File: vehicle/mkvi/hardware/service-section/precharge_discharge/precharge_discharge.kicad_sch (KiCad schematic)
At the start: 13 parts, among them J1 MicroFit_VT_5x1, J2 Automotive_M.2_Edge_Connector, K1 G2RG-2A-X_DC12, K2 3350-4275-126, Q1 SSM3K333R

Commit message: Begin layout add footprints
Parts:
- K1: footprint OEM:G2RG-2A-X -> OEM:G2RG-X
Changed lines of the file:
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@@
     (property "Reference" "K1" (id 0) (at 71.12 43.18 0))
     (property "Value" "G2RG-2A-X_DC12" (id 1) (at 71.12 45.72 0))
-    (property "Footprint" "OEM:G2RG-2A-X" (id 2) (at 71.12 57.15 0)
+    (property "Footprint" "OEM:G2RG-X" (id 2) (at 71.12 57.15 0)
       (effects (font (size 1.27 1.27)) hide)
     )
@@
       (reference "#PWR?") (unit 1) (value "GND") (footprint "")
     )
-    (path "/1d3603a0-934c-404e-9b38-4b65044f588c/607af4f2-91e7-418d-a7ac-4d54e191778d"
-      (reference "C1") (unit 1) (value "10nF") (footprint "")
-    )
-    (path "/aae00dc5-0627-4ce2-bb50-5359aef1b906/607af4f2-91e7-418d-a7ac-4d54e191778d"
-      (reference "C2") (unit 1) (value "10nF") (footprint "")
-    )
-    (path "/f42ceb10-3a39-4caa-a323-2ed850359949/607af4f2-91e7-418d-a7ac-4d54e191778d"
-      (reference "C3") (unit 1) (value "10nF") (footprint "")
+    (path "/1d3603a0-934c-404e-9b38-4b65044f588c/6dc3a5a5-6ba7-45ee-890e-2b247ac5cbfa"
+      (reference "C1") (unit 1) (value "C_10nF") (footprint "footprints:C_1206_OEM")
+    )
+    (path "/aae00dc5-0627-4ce2-bb50-5359aef1b906/6dc3a5a5-6ba7-45ee-890e-2b247ac5cbfa"
+      (reference "C2") (unit 1) (value "C_10nF") (footprint "footprints:C_1206_OEM")
+    )
+    (path "/f42ceb10-3a39-4caa-a323-2ed850359949/6dc3a5a5-6ba7-45ee-890e-2b247ac5cbfa"
+      (reference "C3") (unit 1) (value "C_10nF") (footprint "footprints:C_1206_OEM")
     )
     (path "/13199f4f-49d4-4127-8a75-8da39b0b7cb9"
@@
     )
     (path "/06e0ac0e-a0c5-4a6c-9061-994da59b167d"
-      (reference "K1") (unit 1) (value "G2RG-2A-X_DC12") (footprint "OEM:G2RG-2A-X")
+      (reference "K1") (unit 1) (value "G2RG-2A-X_DC12") (footprint "OEM:G2RG-X")
     )
     (path "/1c839dd3-e0c7-4808-b8be-0e8fc2ef2cdb"
@@
     )
     (path "/1d3603a0-934c-404e-9b38-4b65044f588c/ca7852e4-64fa-4c30-bad9-fbe9a1ffbb05"
-      (reference "TH1") (unit 1) (value "Thermistor") (footprint "")
+      (reference "TH1") (unit 1) (value "Thermistor") (footprint "footprints:Thermistor")
     )
     (path "/aae00dc5-0627-4ce2-bb50-5359aef1b906/ca7852e4-64fa-4c30-bad9-fbe9a1ffbb05"
-      (reference "TH2") (unit 1) (value "Thermistor") (footprint "")
+      (reference "TH2") (unit 1) (value "Thermistor") (footprint "footprints:Thermistor")
     )
     (path "/f42ceb10-3a39-4caa-a323-2ed850359949/ca7852e4-64fa-4c30-bad9-fbe9a1ffbb05"
-      (reference "TH3") (unit 1) (value "Thermistor") (footprint "")
+      (reference "TH3") (unit 1) (value "Thermistor") (footprint "footprints:Thermistor")
     )
     (path "/1d3603a0-934c-404e-9b38-4b65044f588c/1d731957-08e8-4a84-bf4b-f84aa0692269"

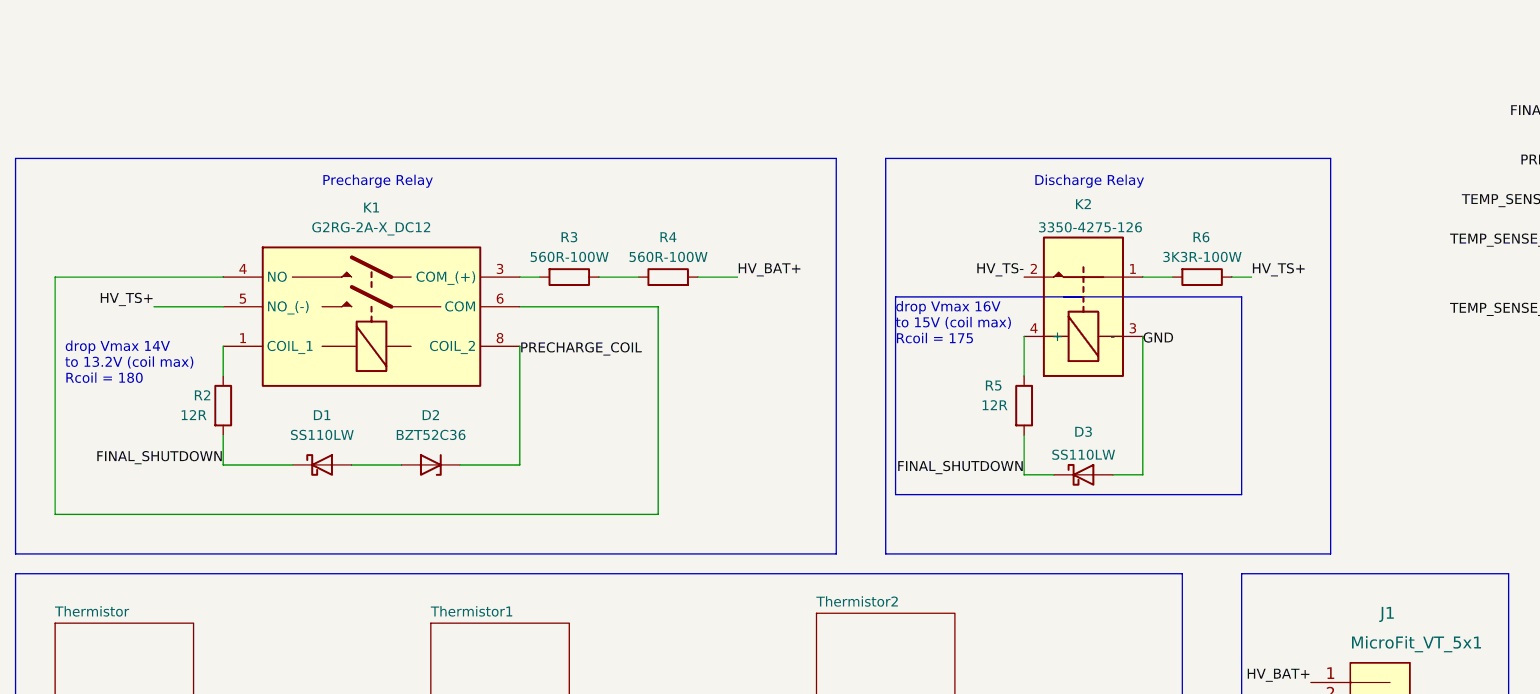
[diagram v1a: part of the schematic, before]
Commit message: Rev.3 Precharge_Discharge Schematic
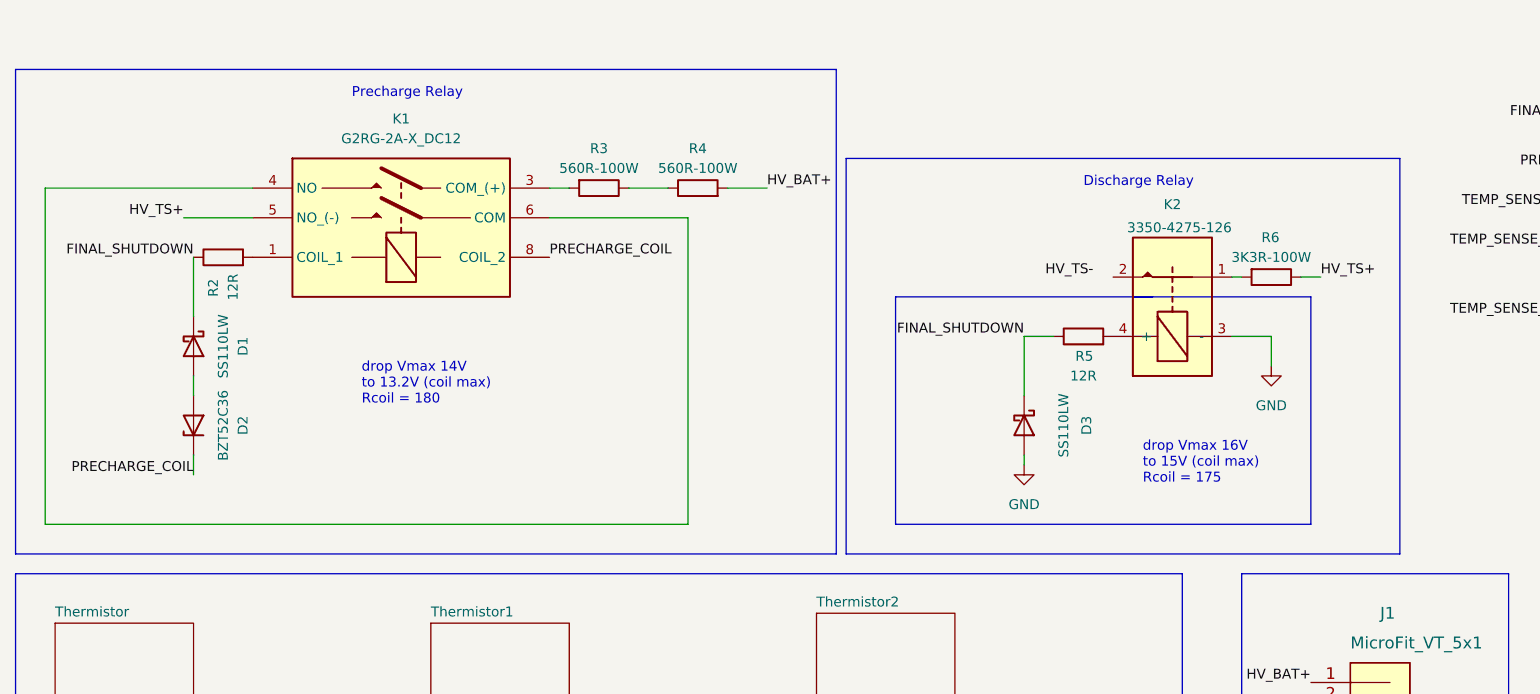
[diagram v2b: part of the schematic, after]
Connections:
- net FINAL_SHUTDOWN: now also R2.1, R5.1; no longer R2.2, R5.2
- net HV_TS-: no longer K2.2
- net at K1.1 (COIL_1): now also R2.2; no longer R2.1
- net at K2.4 (+): now also R5.2; no longer R5.1
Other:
- moved on the sheet: D1, D2, D3, K1, K2, R2, R3, R4, R5, R6

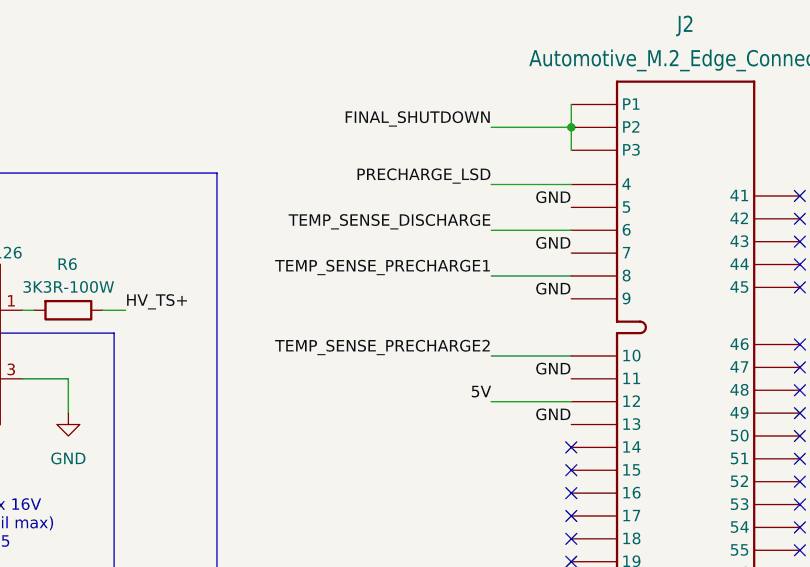
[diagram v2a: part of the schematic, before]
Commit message: V1. Precharge_Discharge PCB Layout
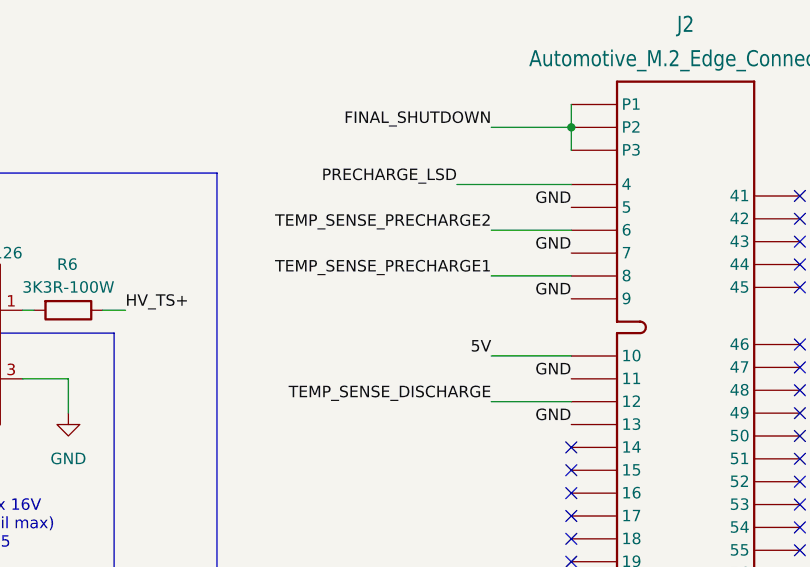
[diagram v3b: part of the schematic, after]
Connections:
- net +5V: now also J2.10; no longer J2.12
- net TEMP_SENSE_DISCHARGE: now also J2.12; no longer J2.6
- net TEMP_SENSE_PRECHARGE2: now also J2.6; no longer J2.10
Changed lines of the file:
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@@
     (stroke (width 0) (type default) (color 0 0 0 0))
   )
-  (wire (pts (xy 233.68 38.1) (xy 242.57 38.1))
+  (wire (pts (xy 229.87 38.1) (xy 242.57 38.1))
     (stroke (width 0) (type default) (color 0 0 0 0))
   )
@@
     (effects (font (size 1.27 1.27)) (justify left bottom))
   )
-  (label "5V" (at 233.68 62.23 180)
+  (label "TEMP_SENSE_DISCHARGE" (at 233.68 62.23 180)
     (effects (font (size 1.27 1.27)) (justify right bottom))
   )
@@
     (effects (font (size 1.27 1.27)) (justify right bottom))
   )
-  (label "TEMP_SENSE_DISCHARGE" (at 233.68 43.18 180)
+  (label "TEMP_SENSE_PRECHARGE2" (at 233.68 43.18 180)
     (effects (font (size 1.27 1.27)) (justify right bottom))
   )
@@
     (effects (font (size 1.27 1.27)) (justify left bottom))
   )
-  (label "TEMP_SENSE_PRECHARGE2" (at 233.68 57.15 180)
+  (label "5V" (at 233.68 57.15 180)
     (effects (font (size 1.27 1.27)) (justify right bottom))
   )
@@
     (effects (font (size 1.27 1.27)) (justify right bottom))
   )
-  (label "PRECHARGE_LSD" (at 233.68 38.1 180)
-    (effects (font (size 1.27 1.27)) (justify right bottom))
-  )
+  (label "PRECHARGE_LSD" (at 229.87 38.1 180)
+    (effects (font (size 1.27 1.27)) (justify right bottom))
+  )

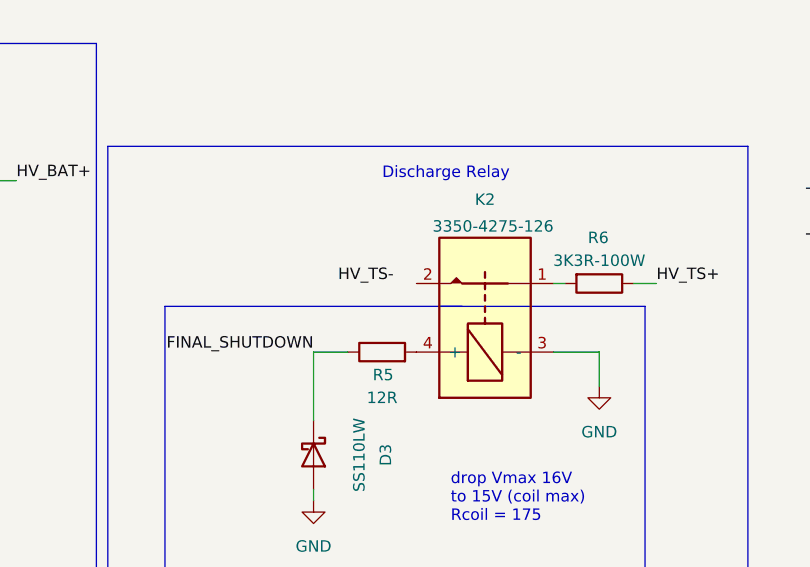
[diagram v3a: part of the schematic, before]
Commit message: feat: updates from layout checklist
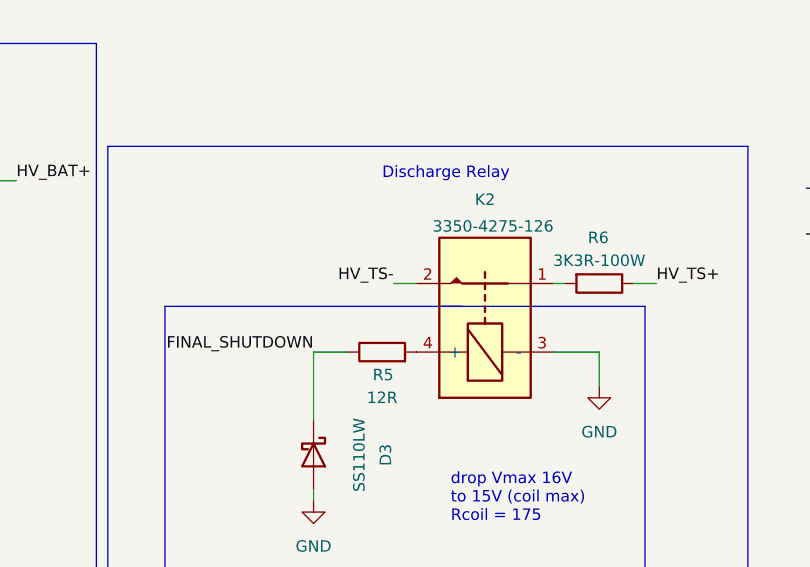
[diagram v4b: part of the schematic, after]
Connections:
- net HV_TS-: now also K2.2
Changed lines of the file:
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@@
+    (stroke (width 0) (type default) (color 0 0 0 0))
+  )
+  (wire (pts (xy 163.83 52.07) (xy 166.37 52.07))
     (stroke (width 0) (type default) (color 0 0 0 0))
   )
@@
   )
   (symbol_instances
+    (path "/61fcfc8d-80a4-4ffc-b730-9f17fc90d2e2"
+      (reference "#PWR?") (unit 1) (value "GND") (footprint "")
+    )
+    (path "/4e074b05-b4d4-46e8-b6a4-6079f1f04f3c"
+      (reference "#PWR?") (unit 1) (value "GND") (footprint "")
+    )
+    (path "/39fb457f-45e0-4faa-b286-55e2425f34ba"
+      (reference "#PWR?") (unit 1) (value "GND") (footprint "")
+    )
     (path "/18930298-950b-43f3-992d-121e7a00145a"
       (reference "#PWR?") (unit 1) (value "GND") (footprint "")
@@
       (reference "#PWR?") (unit 1) (value "+5V") (footprint "")
     )
-    (path "/39fb457f-45e0-4faa-b286-55e2425f34ba"
-      (reference "#PWR?") (unit 1) (value "GND") (footprint "")
+    (path "/1d3603a0-934c-404e-9b38-4b65044f588c/a178f5c8-b4bb-4143-aeb6-2cae7a246fa0"
+      (reference "#PWR?") (unit 1) (value "+5V") (footprint "")
     )
     (path "/1d3603a0-934c-404e-9b38-4b65044f588c/80d772a7-c654-45d6-8d16-7b789d3c1039"
       (reference "#PWR?") (unit 1) (value "+5V") (footprint "")
     )
-    (path "/1d3603a0-934c-404e-9b38-4b65044f588c/a178f5c8-b4bb-4143-aeb6-2cae7a246fa0"
+    (path "/1d3603a0-934c-404e-9b38-4b65044f588c/a2a80cf1-64e7-4004-9710-deb7f131cb2a"
+      (reference "#PWR?") (unit 1) (value "GND") (footprint "")
+    )
+    (path "/1d3603a0-934c-404e-9b38-4b65044f588c/ab021d4c-2de5-4da2-b018-19ab9a4b838b"
+      (reference "#PWR?") (unit 1) (value "GND") (footprint "")
+    )
+    (path "/1d3603a0-934c-404e-9b38-4b65044f588c/3b9fedc3-8004-49ad-a3fe-28afa1ea394b"
+      (reference "#PWR?") (unit 1) (value "GND") (footprint "")
+    )
+    (path "/aae00dc5-0627-4ce2-bb50-5359aef1b906/a178f5c8-b4bb-4143-aeb6-2cae7a246fa0"
       (reference "#PWR?") (unit 1) (value "+5V") (footprint "")
-    )
-    (path "/1d3603a0-934c-404e-9b38-4b65044f588c/a2a80cf1-64e7-4004-9710-deb7f131cb2a"
-      (reference "#PWR?") (unit 1) (value "GND") (footprint "")
-    )
-    (path "/1d3603a0-934c-404e-9b38-4b65044f588c/ab021d4c-2de5-4da2-b018-19ab9a4b838b"
-      (reference "#PWR?") (unit 1) (value "GND") (footprint "")
-    )
-    (path "/1d3603a0-934c-404e-9b38-4b65044f588c/3b9fedc3-8004-49ad-a3fe-28afa1ea394b"
-      (reference "#PWR?") (unit 1) (value "GND") (footprint "")
     )
     (path "/aae00dc5-0627-4ce2-bb50-5359aef1b906/80d772a7-c654-45d6-8d16-7b789d3c1039"
       (reference "#PWR?") (unit 1) (value "+5V") (footprint "")
     )
-    (path "/aae00dc5-0627-4ce2-bb50-5359aef1b906/a178f5c8-b4bb-4143-aeb6-2cae7a246fa0"
+    (path "/aae00dc5-0627-4ce2-bb50-5359aef1b906/a2a80cf1-64e7-4004-9710-deb7f131cb2a"
+      (reference "#PWR?") (unit 1) (value "GND") (footprint "")
+    )
+    (path "/aae00dc5-0627-4ce2-bb50-5359aef1b906/ab021d4c-2de5-4da2-b018-19ab9a4b838b"
+      (reference "#PWR?") (unit 1) (value "GND") (footprint "")
+    )
+    (path "/aae00dc5-0627-4ce2-bb50-5359aef1b906/3b9fedc3-8004-49ad-a3fe-28afa1ea394b"
+      (reference "#PWR?") (unit 1) (value "GND") (footprint "")
+    )
+    (path "/f42ceb10-3a39-4caa-a323-2ed850359949/a178f5c8-b4bb-4143-aeb6-2cae7a246fa0"
       (reference "#PWR?") (unit 1) (value "+5V") (footprint "")
-    )
-    (path "/aae00dc5-0627-4ce2-bb50-5359aef1b906/a2a80cf1-64e7-4004-9710-deb7f131cb2a"
-      (reference "#PWR?") (unit 1) (value "GND") (footprint "")
-    )
-    (path "/aae00dc5-0627-4ce2-bb50-5359aef1b906/ab021d4c-2de5-4da2-b018-19ab9a4b838b"
-      (reference "#PWR?") (unit 1) (value "GND") (footprint "")
-    )
-    (path "/aae00dc5-0627-4ce2-bb50-5359aef1b906/3b9fedc3-8004-49ad-a3fe-28afa1ea394b"
-      (reference "#PWR?") (unit 1) (value "GND") (footprint "")
     )
     (path "/f42ceb10-3a39-4caa-a323-2ed850359949/80d772a7-c654-45d6-8d16-7b789d3c1039"
       (reference "#PWR?") (unit 1) (value "+5V") (footprint "")
     )
-    (path "/f42ceb10-3a39-4caa-a323-2ed850359949/a178f5c8-b4bb-4143-aeb6-2cae7a246fa0"
-      (reference "#PWR?") (unit 1) (value "+5V") (footprint "")
-    )
     (path "/f42ceb10-3a39-4caa-a323-2ed850359949/a2a80cf1-64e7-4004-9710-deb7f131cb2a"
       (reference "#PWR?") (unit 1) (value "GND") (footprint "")
@@
       (reference "#PWR?") (unit 1) (value "GND") (footprint "")
     )
-    (path "/4e074b05-b4d4-46e8-b6a4-6079f1f04f3c"
-      (reference "#PWR?") (unit 1) (value "GND") (footprint "")
-    )
-    (path "/61fcfc8d-80a4-4ffc-b730-9f17fc90d2e2"
+    (path "/1d3603a0-934c-404e-9b38-4b65044f588c/90dd3af5-4ce0-4209-b124-e700e1d8b918"
+      (reference "#PWR?") (unit 1) (value "GND") (footprint "")
+    )
+    (path "/aae00dc5-0627-4ce2-bb50-5359aef1b906/90dd3af5-4ce0-4209-b124-e700e1d8b918"
+      (reference "#PWR?") (unit 1) (value "GND") (footprint "")
+    )
+    (path "/f42ceb10-3a39-4caa-a323-2ed850359949/90dd3af5-4ce0-4209-b124-e700e1d8b918"
       (reference "#PWR?") (unit 1) (value "GND") (footprint "")
     )
@@
       (reference "C3") (unit 1) (value "C_10nF") (footprint "footprints:C_1206_OEM")
     )
+    (path "/1d3603a0-934c-404e-9b38-4b65044f588c/b7179219-a351-4b12-a22c-747945b7713d"
+      (reference "C4") (unit 1) (value "C_0.1uF") (footprint "footprints:C_0805_OEM")
+    )
+    (path "/aae00dc5-0627-4ce2-bb50-5359aef1b906/b7179219-a351-4b12-a22c-747945b7713d"
+      (reference "C5") (unit 1) (value "C_0.1uF") (footprint "footprints:C_0805_OEM")
+    )
+    (path "/f42ceb10-3a39-4caa-a323-2ed850359949/b7179219-a351-4b12-a22c-747945b7713d"
+      (reference "C6") (unit 1) (value "C_0.1uF") (footprint "footprints:C_0805_OEM")
+    )
     (path "/13199f4f-49d4-4127-8a75-8da39b0b7cb9"
